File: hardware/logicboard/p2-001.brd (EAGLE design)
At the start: 72 x 72 mm, 29 parts, among them IC1 5V, IC2 74LS07N, IC3 4066N, K1 G5V1, T1 2SC1815, U1 DS18B20

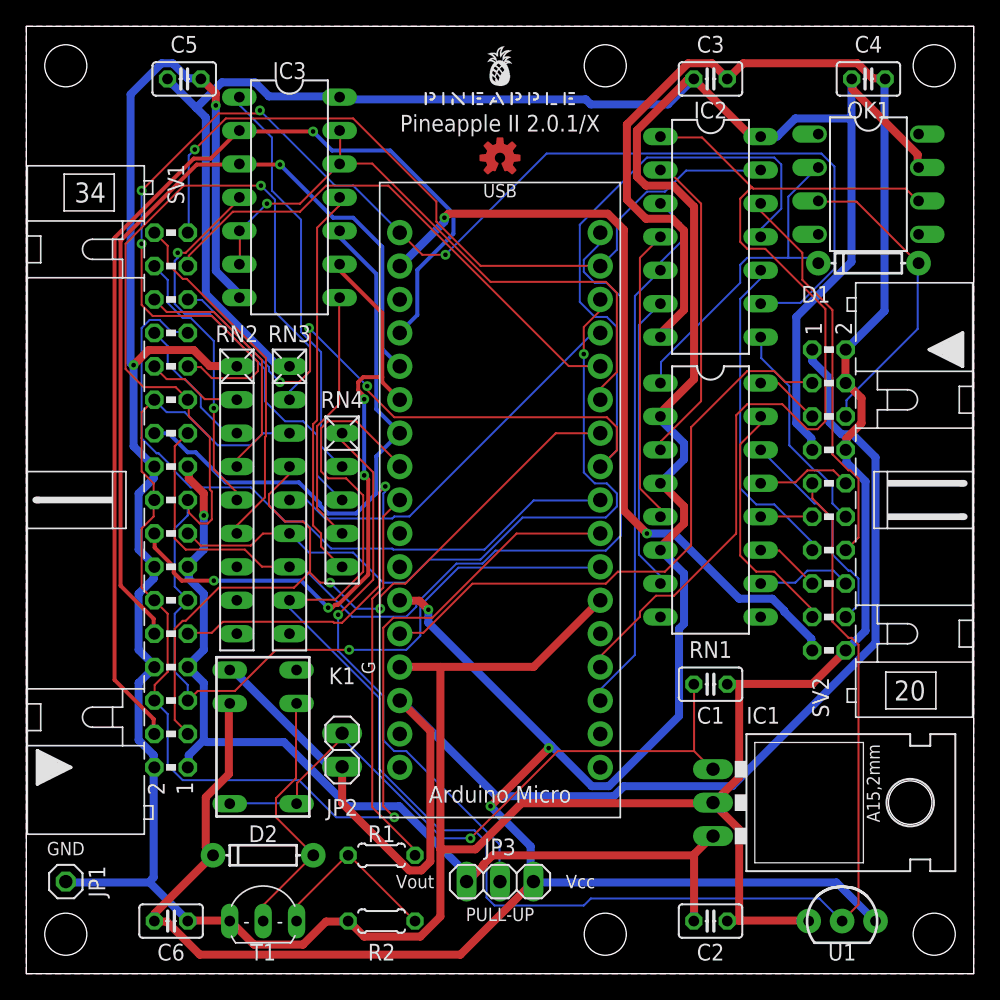
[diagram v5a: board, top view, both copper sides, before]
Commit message: Jumper -> SW.
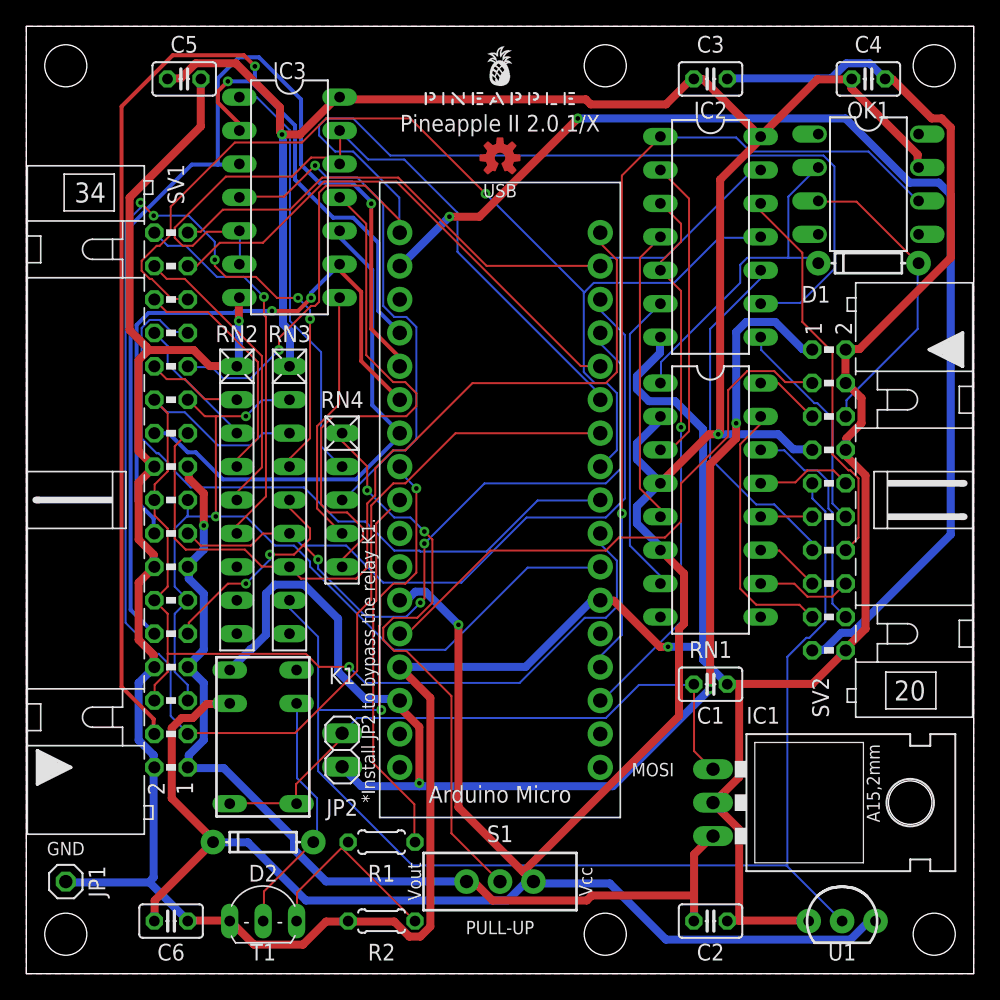
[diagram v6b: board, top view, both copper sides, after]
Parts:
- removed JP3: (no value), pinhead:1X03
- added S1: (no value), SparkFun-Switches:SWITCH_SPDT_PTH_11.6X4.0MM
- moved D2 1.00 mm to (18.0, 10.0)
- moved R1 1.00 mm to (27.0, 10.0)
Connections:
- removed net N$2: JP3.2, RN4.1
- new net VPULLUP: RN4.1, S1.2
- net VCC: now also S1.3; no longer JP3.3
- net VOUT: now also S1.1; no longer JP3.1
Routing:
- net D1: track 60.5 -> 120.3 mm, vias 2 -> 5
- net VPULLUP: track 0.00 -> 44.5 mm, vias 0 -> 2
- net N$2: track 41.8 -> 0.00 mm, vias 1 -> 0
- net SDA: track 112.7 -> 71.7 mm
- net VDD: track 59.9 -> 88.9 mm
- net VCC: track 300.6 -> 275.1 mm
- net GND: track 313.9 -> 291.3 mm
- net A2: track 65.5 -> 81.7 mm
- net SCL: track 95.8 -> 81.0 mm
- net RX: track 75.7 -> 63.9 mm, vias 0 -> 1
- net A1: track 81.5 -> 93.3 mm, vias 1 -> 2
- net N$6: track 29.9 -> 40.1 mm
- net LED2: track 90.4 -> 80.6 mm, vias 3 -> 1
- net LED4: track 60.3 -> 51.1 mm, vias 1 -> 0
- net PULLUP: track 48.7 -> 57.1 mm, vias 1 -> 0
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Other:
- board text added: "*Install JP2 to bypass the relay K1."
- board text added: "MOSI"
- board text removed: "G"

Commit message: Changed netclass of VPULLUP to power.
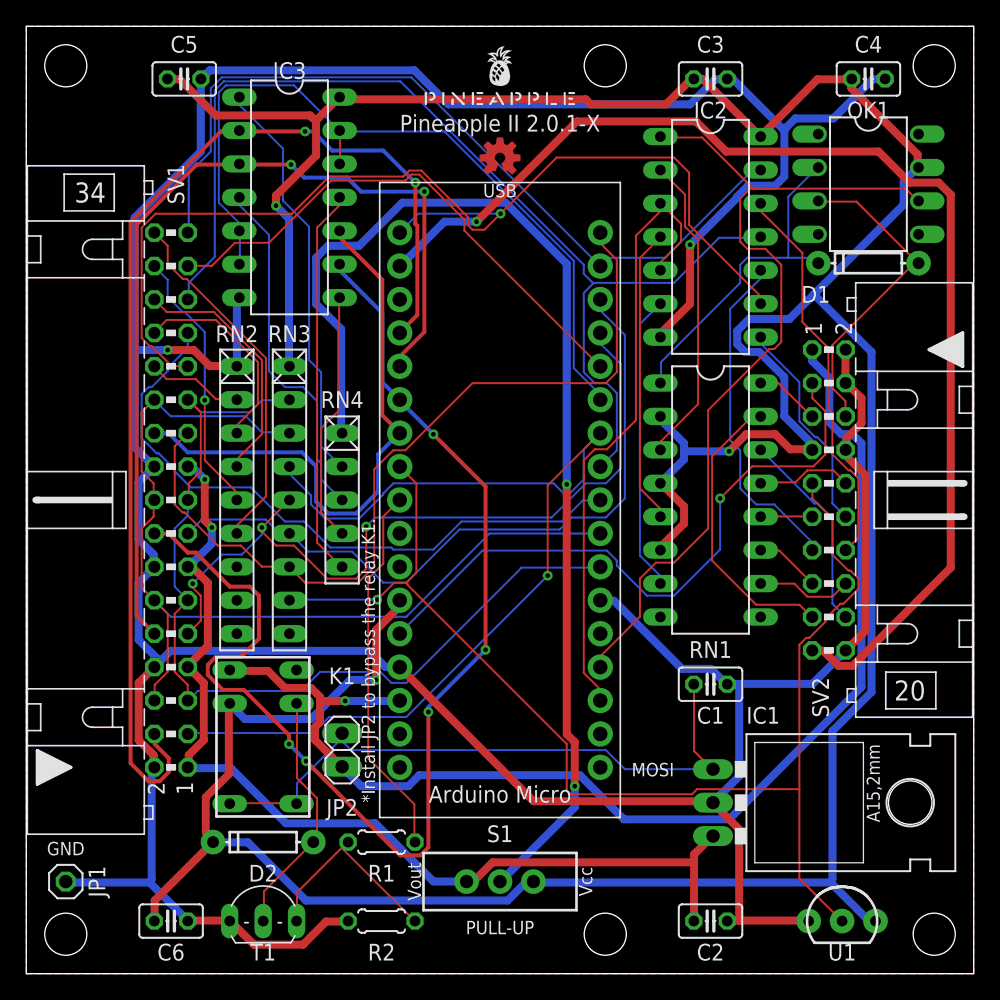
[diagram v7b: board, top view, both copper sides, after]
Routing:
- net A3: track 46.2 -> 92.4 mm, vias 2 -> 5
- net D1: track 120.3 -> 75.4 mm, vias 5 -> 1
- net VPULLUP: track 44.5 -> 86.4 mm
- net THS: track 114.9 -> 96.2 mm, vias 2 -> 1
- net LED0: track 96.8 -> 81.6 mm
- net N$4: track 40.2 -> 27.1 mm, vias 1 -> 0
- net GND: track 291.3 -> 304.1 mm
- net LED4: track 51.1 -> 62.8 mm
- net A2: track 81.7 -> 70.3 mm, vias 1 -> 2
- net N$6: track 40.1 -> 29.6 mm
- net VCC: track 275.1 -> 284.6 mm
- net SCL: track 81.0 -> 73.7 mm, vias 1 -> 0
- net A1: track 93.3 -> 86.4 mm
- net TX: track 42.4 -> 47.9 mm, vias 1 -> 0
- net RST: track 43.8 -> 49.2 mm, vias 0 -> 1
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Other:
- board text added: "Pineapple II 2.0.1-X"
- board text removed: "Pineapple II 2.0.1/X"

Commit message: Replaced back-panel SW to LEDSW. Now Back port is incompatible to 2.0.0-X.
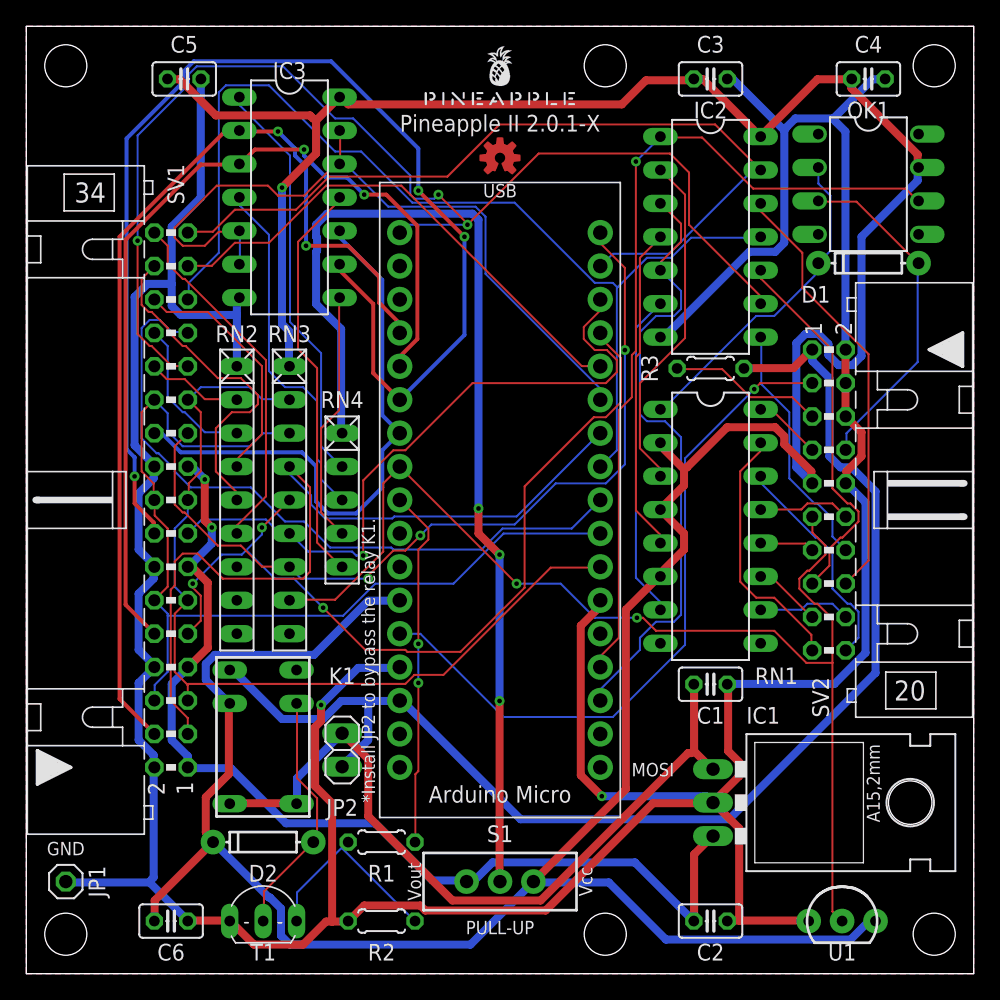
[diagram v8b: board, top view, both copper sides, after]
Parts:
- added R3: 1k, resistor:0204/5
- moved RN1 2.00 mm to (52.0, 34.0)
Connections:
- net N$1 renamed V+12V
- removed net VDD: MC1.P$33, SV2.19
- new net PWRLED: R3.1, SV2.5
- net +12V: now also R3.2
- net GND: now also SV2.10, SV2.6; no longer SV2.20, SV2.8
- net MINRTN: now also SV2.8; no longer SV2.6
- net MINSND: now also SV2.7; no longer SV2.5
- net MO1RTN: now also SV2.13; no longer SV2.11
- net MO1SND: now also SV2.12; no longer SV2.10
- net MO2RTN: now also SV2.18; no longer SV2.16
- net MO2SND: now also SV2.17; no longer SV2.15
- net MTHRTN: now also SV2.20; no longer SV2.18
- net MTHSND: now also SV2.19; no longer SV2.17
- net THS: now also SV2.11; no longer SV2.9
- net VCC: now also SV2.9; no longer SV2.7
- net XLEDB: now also SV2.15; no longer SV2.13
- net XLEDG: now also SV2.14; no longer SV2.12
- net XLEDR: now also SV2.16; no longer SV2.14
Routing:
- net VDD: track 91.2 -> 0.00 mm, vias 1 -> 0
- net D1: track 75.4 -> 62.6 mm, vias 1 -> 0
- net PWRLED: track 0.00 -> 11.8 mm
- net A1: track 86.4 -> 75.3 mm
- net VCC: track 284.6 -> 274.9 mm, vias 3 -> 1
- net V+12V: track 48.7 -> 58.3 mm
- net LED0: track 81.6 -> 91.1 mm, vias 1 -> 3
- net THS: track 96.2 -> 88.2 mm, vias 1 -> 2
- net VPULLUP: track 86.4 -> 80.6 mm, vias 2 -> 3
- net LED3K: track 20.5 -> 25.9 mm, vias 1 -> 0
- net D2: track 60.2 -> 64.7 mm
- net +12V: track 93.8 -> 98.2 mm, vias 1 -> 0
- net LED1K: track 15.7 -> 11.7 mm
- net RST: track 49.2 -> 52.8 mm
- net RX: track 67.3 -> 63.9 mm, vias 0 -> 1
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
